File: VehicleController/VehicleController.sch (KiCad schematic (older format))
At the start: 9 parts

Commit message: Updates all around
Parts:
- removed BT?: Battery, symbol Battery
- removed D?: D_Schottky, symbol D_Schottky
- removed F?: Polyfuse, symbol Polyfuse
- removed R? (x3): R, symbol R
- removed U?: TL431, symbol TL431
- removed U?: BTS6133D, symbol BTS6133D
- removed U?: Teensy_3.5, symbol Teensy_3.5
- added C? (x3): C_Small, symbol C_Small
- added J1, J?: RJ45, symbol RJ45
- added P1: CONN_02X02, symbol CONN_02X02
- added P? (x2): CONN_02X12, symbol CONN_02X12
- added P?: CONN_01X02, symbol CONN_01X02
- added U?: Teensy_3.5, symbol Teensy_3.5
- added U?: AP1117, TO_SOT_Packages_SMD:SOT-223, symbol AP1117
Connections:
- net labels added: +12V, +3.3V, +5V, CANH, CANL, CurrentSense
- wire segments 16 -> 38

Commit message: Vehicle Controller updates
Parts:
- removed C? (x2): C_Small, symbol C_Small
- removed J1, J?: RJ45, symbol RJ45
- removed P? (x2): CONN_02X12, symbol CONN_02X12
- removed U?: AP1117, TO_SOT_Packages_SMD:SOT-223, symbol AP1117
- added BT?: Battery_Cell, symbol Battery_Cell
- added C1: C_Small, symbol C_Small
- added P3: RPi_USB_PWR, symbol USB_A
- added P5: SMALL_SIG_MX150, symbol CONN_02X16
- P2: renamed from P?; value CONN_01X02 -> BATT_IN
- gave numbers to parts that had none: 2
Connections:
- net labels added: 3D-FIX, 3D_FIX, CANRX, CANTX, GPS_RX, GPS_TX, SCL0, SDA0
- net labels removed: CANH, CANL
- wire segments 38 -> 45
- no-connect marks 0 -> 5
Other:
- moved on the sheet: C2, P2, U1

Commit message: Added SENtral Fusion Hub to VC Schematic
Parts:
- added U?: UltimateSensorFusion, symbol UltimateSensorFusion
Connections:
- net labels added: CS0, MISO0, MOSI0, SCK0
- wire segments 45 -> 60
- no-connect marks 5 -> 10
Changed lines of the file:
@@
-$EndComp
-$Comp
-L +3.3V #PWR05
-U 1 1 587CCB3B
-P 4200 3900
-F 0 "#PWR05" H 4200 3750 50  0001 C CNN
-F 1 "+3.3V" H 4215 4073 50  0000 C CNN
-F 2 "" H 4200 3900 50  0000 C CNN
-F 3 "" H 4200 3900 50  0000 C CNN
-	1    4200 3900
-	1    0    0    -1
 $EndComp
 $Comp
@@
 Text Label 7100 2800 2    60   ~ 0
 +3.3V
-Text Label 7050 4000 2    60   ~ 0
+Text Label 7400 4000 2    60   ~ 0
 GND
 NoConn ~ 6750 2700
@@
 NoConn ~ 6750 4100
 NoConn ~ 6750 4200
-Text Label 7050 3300 2    60   ~ 0
+Text Label 7100 3300 2    60   ~ 0
 SCL0
-Text Label 7050 3400 2    60   ~ 0
+Text Label 7100 3400 2    60   ~ 0
 SDA0
 Wire Wire Line
@@
 	2400 3300 2400 3400
 Wire Wire Line
-	2050 3300 2400 3300
+	2050 3300 2250 3300
+Wire Wire Line
+	2250 3300 2400 3300
 Wire Wire Line
 	1650 3600 1650 3500
@@
 	2400 3000 2400 2900
 Wire Wire Line
-	2050 3000 2400 3000
-Wire Wire Line
-	4200 4000 4200 3900
-Wire Wire Line
-	4550 4000 4200 4000
+	2050 3000 2250 3000
+Wire Wire Line
+	2250 3000 2400 3000
+Wire Wire Line
+	4550 4000 3550 4000
 Wire Wire Line
 	7350 2600 7350 2650
@@
 Connection ~ 6900 2600
 Wire Wire Line
-	6750 2600 7050 2600
+	6750 2600 6900 2600
+Wire Wire Line
+	6900 2600 7050 2600
 Wire Wire Line
 	6900 2400 6900 2600
@@
 	2300 2150 2400 2150
 Wire Wire Line
-	2400 2050 2400 2250
+	2400 2050 2400 2150
+Wire Wire Line
+	2400 2150 2400 2250
 Wire Wire Line
 	2300 2050 2400 2050
@@
 	1650 2050 1800 2050
 Wire Wire Line
-	1650 1900 1650 2150
+	1650 1900 1650 2050
+Wire Wire Line
+	1650 2050 1650 2150
 Wire Wire Line
 	4200 2600 4550 2600
@@
 	6750 2800 7100 2800
 Wire Wire Line
-	7050 4000 6750 4000
+	7400 4000 6750 4000
 Wire Wire Line
 	4550 3000 4200 3000
@@
 	4550 3100 4200 3100
 Wire Wire Line
-	6750 3300 7050 3300
-Wire Wire Line
-	7050 3400 6750 3400
+	6750 3300 8000 3300
+Wire Wire Line
+	8000 3400 6750 3400
 $Comp
 L Battery_Cell BT?
@@
 Text Label 9400 2200 0    60   ~ 0
 CANRX
+$Comp
+L UltimateSensorFusion U?
+U 1 1 58B0145C
+P 8550 3400
+F 0 "U?" H 8550 3887 60  0000 C CNN
+F 1 "UltimateSensorFusion" H 8550 3781 60  0000 C CNN
+F 2 "" H 8550 3300 60  0001 C CNN
+F 3 "" H 8550 3300 60  0001 C CNN
+	1    8550 3400
+	1    0    0    -1
+$EndComp
+$Comp
+L +3.3V #PWR?
+U 1 1 58B0A4BD
+P 7850 3100
+F 0 "#PWR?" H 7850 2950 50  0001 C CNN
+F 1 "+3.3V" H 7865 3273 50  0000 C CNN
+F 2 "" H 7850 3100 50  0000 C CNN
+F 3 "" H 7850 3100 50  0000 C CNN
+	1    7850 3100
+	1    0    0    -1
+$EndComp
+Wire Wire Line
+	7850 3100 7850 3200
+Wire Wire Line
+	7850 3200 8000 3200
+$Comp
+L GND #PWR?
+U 1 1 58B0C04F
+P 7850 3700
+F 0 "#PWR?" H 7850 3450 50  0001 C CNN
+F 1 "GND" H 7855 3527 50  0000 C CNN
+F 2 "" H 7850 3700 50  0000 C CNN
+F 3 "" H 7850 3700 50  0000 C CNN
+	1    7850 3700
+	1    0    0    -1
+$EndComp
+Wire Wire Line
+	7850 3700 7850 3600
+Wire Wire Line
+	7850 3600 8000 3600
+Wire Wire Line
+	8000 3500 6750 3500
+NoConn ~ 9100 3200
+NoConn ~ 9100 3300
+NoConn ~ 9100 3400
+NoConn ~ 9100 3600
+NoConn ~ 9100 3500
+Text Label 7400 3800 2    60   ~ 0
+CurrentSense
+Wire Wire Line
+	7400 3800 6750 3800
+Wire Wire Line
+	3550 4000 3550 3900
+$Comp
+L +3.3V #PWR05
+U 1 1 587CCB3B
+P 3550 3900
+F 0 "#PWR05" H 3550 3750 50  0001 C CNN
+F 1 "+3.3V" H 3565 4073 50  0000 C CNN
+F 2 "" H 3550 3900 50  0000 C CNN
+F 3 "" H 3550 3900 50  0000 C CNN
+	1    3550 3900
+	1    0    0    -1
+$EndComp
+Wire Wire Line
+	4550 3900 4200 3900
+Text Label 4200 3900 0    60   ~ 0
+MISO0
+Text Label 4200 3800 0    60   ~ 0
+MOSI0
+Text Label 4200 3700 0    60   ~ 0
+CS0
+Wire Wire Line
+	4200 3700 4550 3700
+Wire Wire Line
+	4200 3800 4550 3800
+Wire Wire Line
+	6750 3900 7400 3900
+Text Label 7400 3900 2    60   ~ 0
+SCK0
 $EndSCHEMATC

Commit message: Added GPS, DAC, Isolation sheet, buzzer to VC
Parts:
- removed C1: C_Small, symbol C_Small
- removed P1: CONN_02X02, symbol CONN_02X02
- removed P3: RPi_USB_PWR, symbol USB_A
- added C? (x2): C_Small, symbol C_Small
- added D?: D_Zener, symbol D_Zener
- added F?: 1A, symbol Polyfuse_Small
- added P?: Buzzer, symbol CONN_01X02
- added Q? (x2): Q_NMOS_GDS, symbol Q_NMOS_GDS
- added R? (x4): 2.2k, symbol R_Small
- added R? (x3): R_Small, symbol R_Small
- added U?: BTS6133D, symbol BTS6133D
- BT?: value Battery_Cell -> CR1220
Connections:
- net labels added: +SHTDWN, -SHTDWN, BUZZER, DAC_LATCH, IMU_INT, SCL1, SDA1, SHTDWN_SENSE, SHTDWN_SIG
- net labels removed: 3D-FIX
- wire segments 60 -> 89
- no-connect marks 10 -> 12
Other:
- moved on the sheet: BT?, P5, U?

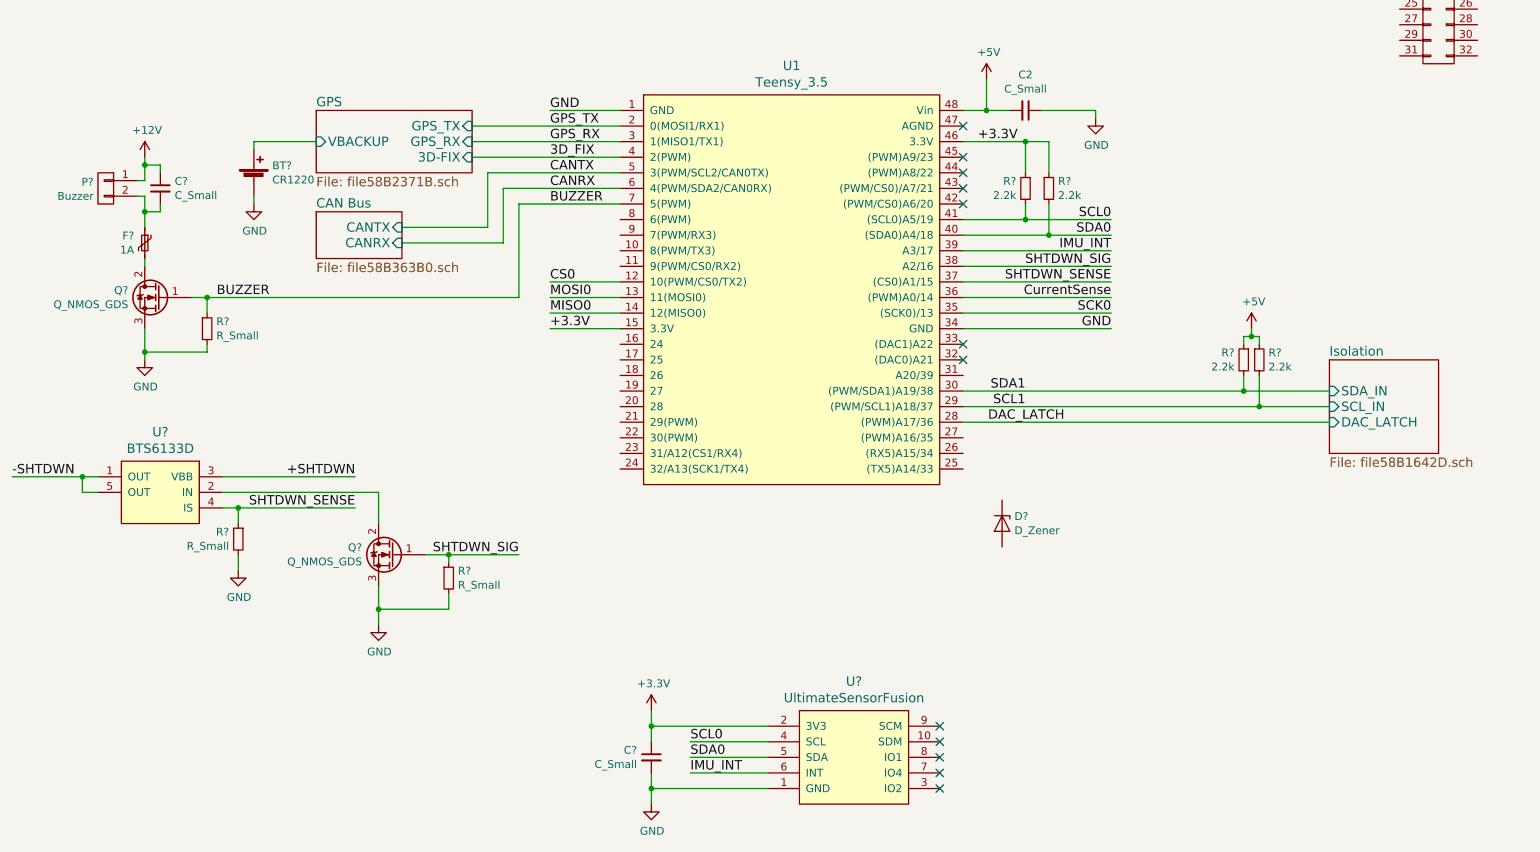
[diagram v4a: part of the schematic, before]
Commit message: Add battery voltage sense, remove i2c pullups for UFS
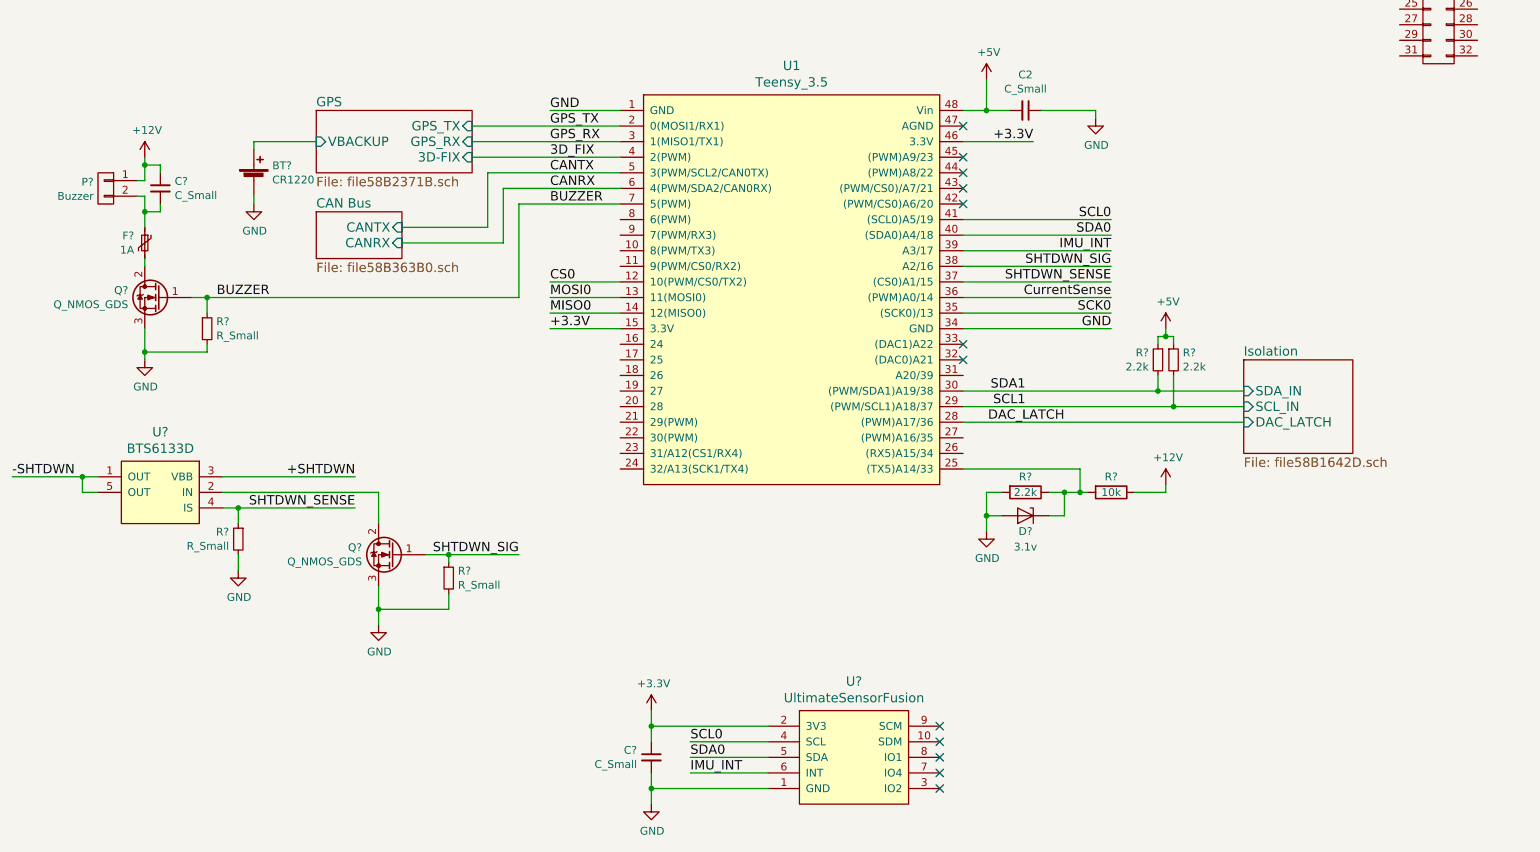
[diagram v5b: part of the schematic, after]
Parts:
- removed D?: D_Zener, symbol D_Zener
- removed R? (x2): 2.2k, symbol R_Small
- added D?: 3.1v, symbol D_Zener
- added R?: 10k, symbol R
- added R?: 2.2k, symbol R
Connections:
- net +12V: now also R?.1
- net GND: now also D?.2 (A), R?.2
- net at U1.25 ((TX5)A14/33): now also D?.1 (K), R?.1, R?.2
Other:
- moved on the sheet: R?

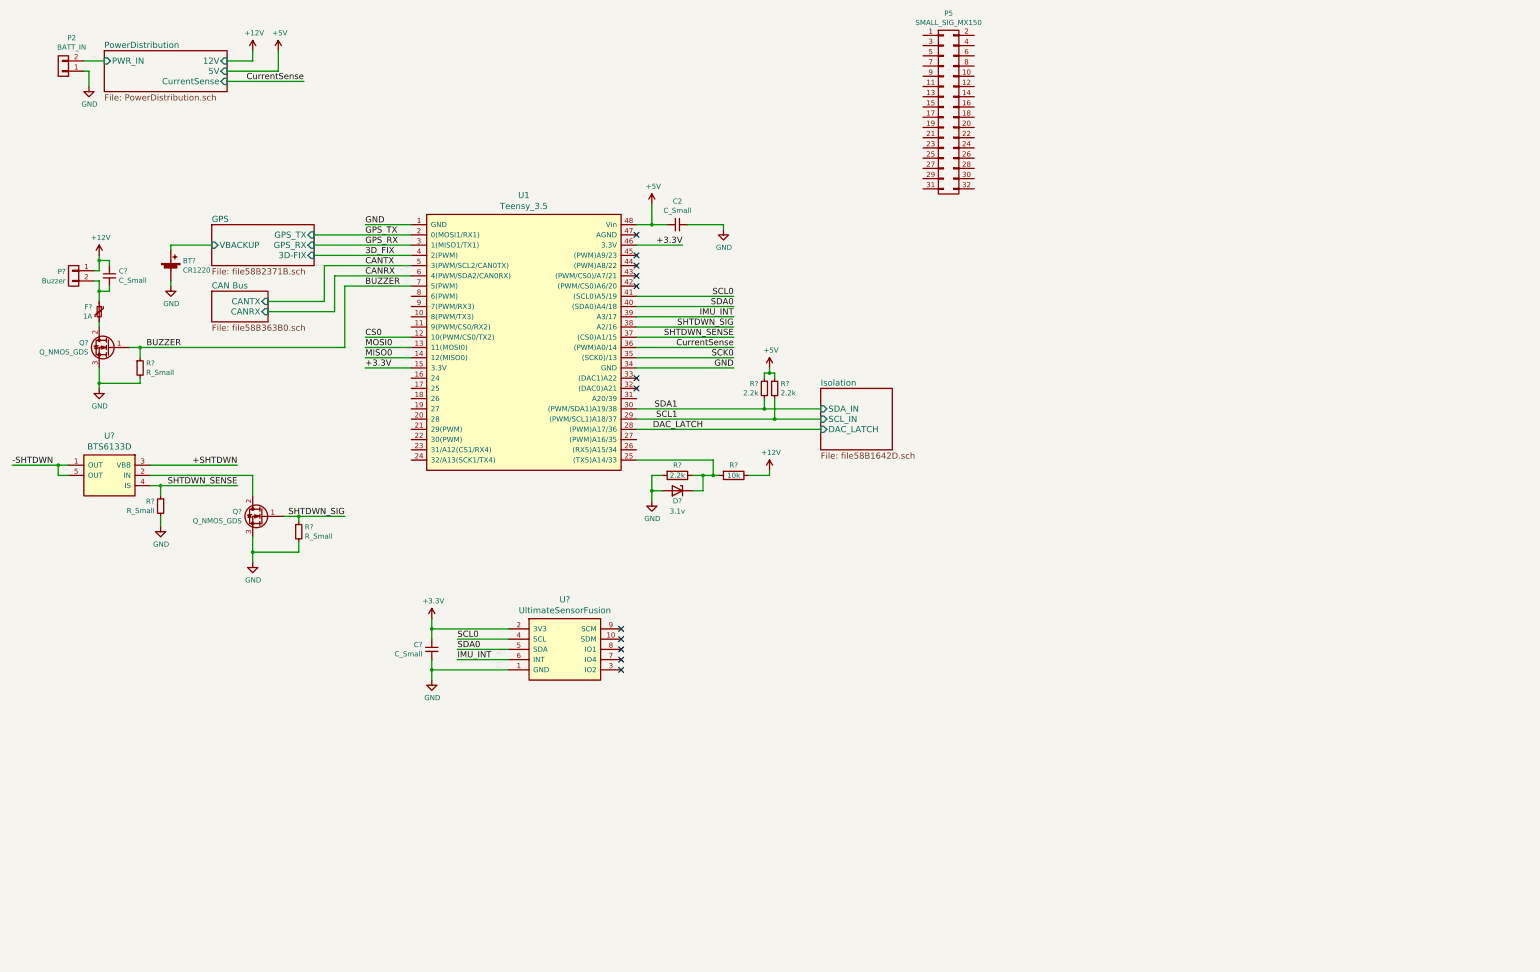
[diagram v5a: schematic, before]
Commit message: 3D model of 16 pin, MX150_8 pin symbol
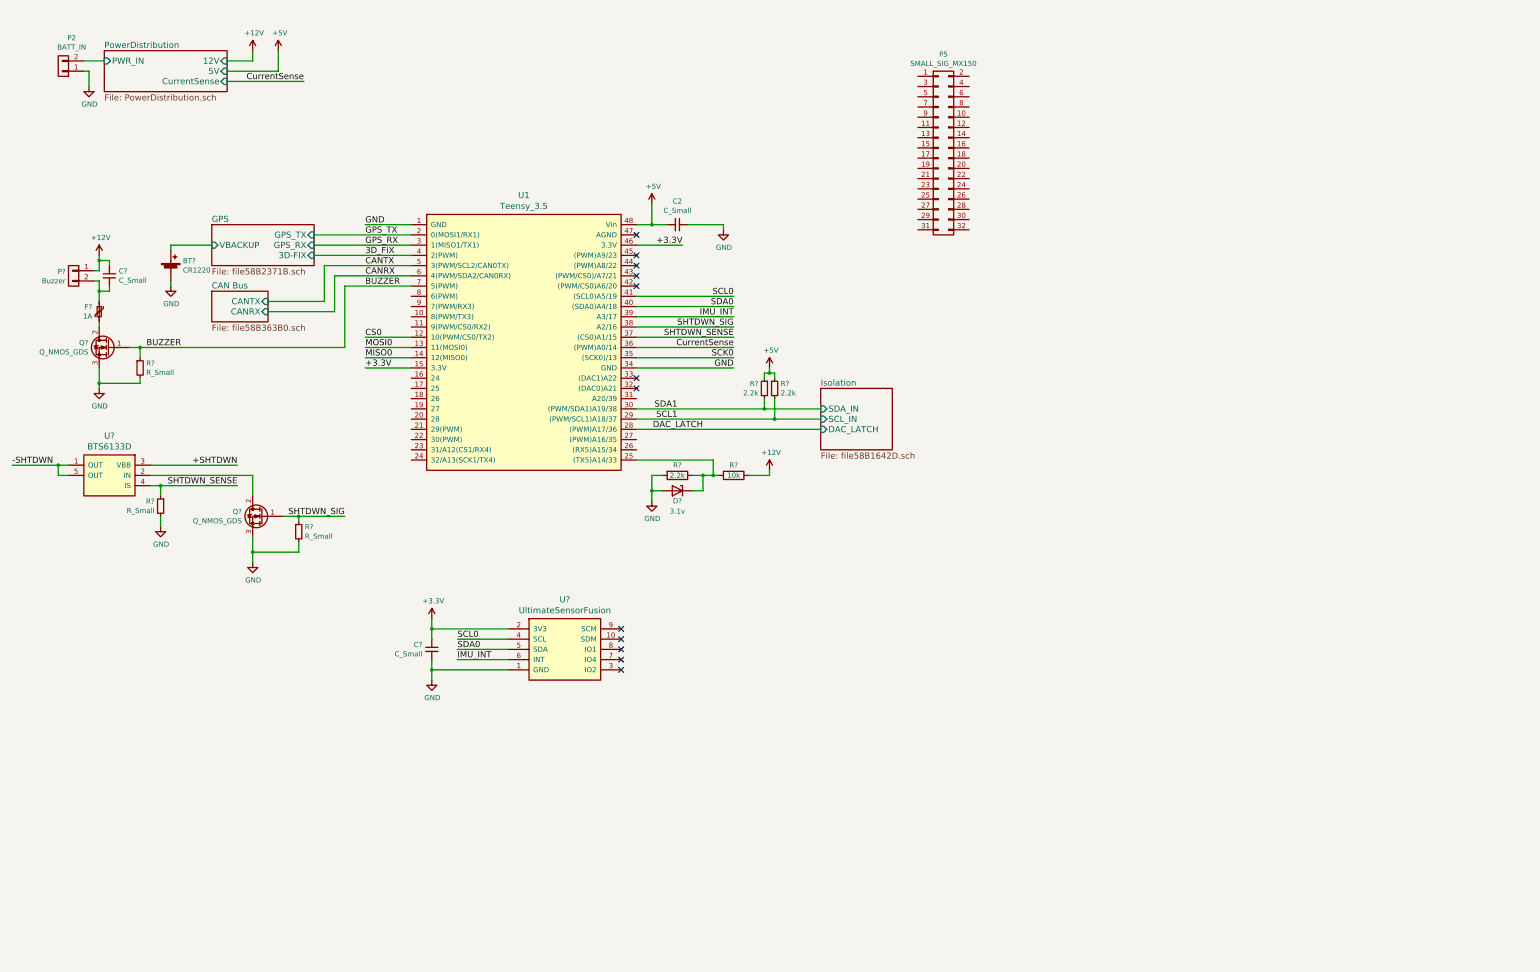
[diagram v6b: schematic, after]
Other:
- moved on the sheet: P5
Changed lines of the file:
@@
 L CONN_02X16 P5
 U 1 1 58AF97B5
-P 9800 1500
-F 0 "P5" H 9800 2465 50  0000 C CNN
-F 1 "SMALL_SIG_MX150" H 9800 2374 50  0000 C CNN
-F 2 "" H 9800 400 50  0000 C CNN
-F 3 "" H 9800 400 50  0000 C CNN
-	1    9800 1500
+P 9750 1900
+F 0 "P5" H 9750 2865 50  0000 C CNN
+F 1 "SMALL_SIG_MX150" H 9750 2774 50  0000 C CNN
+F 2 "" H 9750 800 50  0000 C CNN
+F 3 "" H 9750 800 50  0000 C CNN
+	1    9750 1900
 	1    0    0    -1
 $EndComp
@@
 Connection ~ 6900 2600
 Wire Wire Line
-	6750 2600 6900 2600
-Wire Wire Line
-	6900 2600 7050 2600
+	6750 2600 7050 2600
 Wire Wire Line
 	6900 2400 6900 2600
@@
 	3150 3450 3800 3450
 Wire Wire Line
-	4750 6450 4750 6550
-Wire Wire Line
-	4750 6550 4750 6650
+	4750 6450 4750 6650
 Wire Wire Line
 	4750 6550 5500 6550
 Wire Wire Line
-	4750 6850 4750 6950
-Wire Wire Line
-	4750 6950 4750 7050
+	4750 6850 4750 7050
 Wire Wire Line
 	4750 6950 5500 6950
@@
 	6750 3900 7700 3900
 Wire Wire Line
-	6750 4400 8000 4400
-Wire Wire Line
-	8000 4400 8550 4400
-Wire Wire Line
-	6750 4500 8100 4500
-Wire Wire Line
-	8100 4500 8550 4500
+	6750 4400 8550 4400
+Wire Wire Line
+	6750 4500 8550 4500
 Wire Wire Line
 	6750 4600 8550 4600
 Wire Wire Line
-	8000 4050 8050 4050
-Wire Wire Line
-	8050 4050 8100 4050
+	8000 4050 8100 4050
 Wire Wire Line
 	8100 4050 8100 4100
@@
 Connection ~ 8050 4050
 Wire Wire Line
-	1800 3800 1900 3800
-Wire Wire Line
-	1900 3800 3900 3800
+	1800 3800 3900 3800
 Wire Wire Line
 	1450 3150 1500 3150
 Wire Wire Line
-	1500 3150 1500 3250
-Wire Wire Line
-	1500 3250 1500 3350
-Wire Wire Line
-	1500 4000 1500 4150
-Wire Wire Line
-	1500 4150 1500 4200
+	1500 3150 1500 3350
+Wire Wire Line
+	1500 4000 1500 4200
 Wire Wire Line
 	1500 3600 1500 3600
@@
 	1500 3050 1450 3050
 Wire Wire Line
-	1500 2900 1500 2950
-Wire Wire Line
-	1500 2950 1500 3050
+	1500 2900 1500 3050
 Wire Wire Line
 	3600 2700 4550 2700
@@
 	1500 3550 1500 3600
 Wire Wire Line
-	650  4950 1100 4950
-Wire Wire Line
-	1100 4950 1200 4950
+	650  4950 1200 4950
 Wire Wire Line
 	1200 5050 1100 5050
@@
 	3450 5500 3450 5450
 Wire Wire Line
-	3300 5450 3450 5450
-Wire Wire Line
-	3450 5450 3900 5450
-Wire Wire Line
-	3000 5650 3000 5800
-Wire Wire Line
-	3000 5800 3000 5900
+	3300 5450 3900 5450
+Wire Wire Line
+	3000 5650 3000 5900
 Wire Wire Line
 	3450 5700 3450 5800
@@
 	2100 5250 2100 5150
 Wire Wire Line
-	2000 5150 2100 5150
-Wire Wire Line
-	2100 5150 2850 5150
+	2000 5150 2850 5150
 Wire Wire Line
 	2100 5550 2100 5450
@@
 $EndComp
 Wire Wire Line
-	7300 5050 7400 5050
-Wire Wire Line
-	7400 5050 7500 5050
-Wire Wire Line
-	7500 5050 7550 5050
+	7300 5050 7550 5050
 Wire Wire Line
 	7500 5050 7500 4900
@@
 $EndComp
 Wire Wire Line
-	6900 5050 6900 5200
-Wire Wire Line
-	6900 5200 6900 5300
+	6900 5050 6900 5300
 Wire Wire Line
 	6900 5050 7000 5050

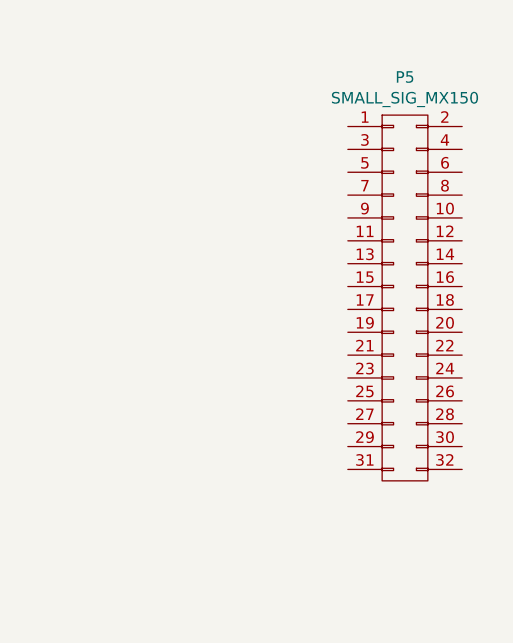
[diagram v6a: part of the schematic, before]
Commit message: Add MX150 8 pin, add Motor Controller connector
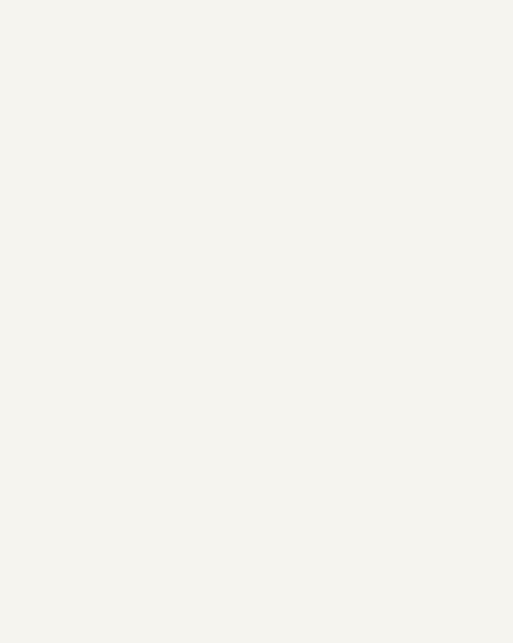
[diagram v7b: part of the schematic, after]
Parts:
- removed P5: SMALL_SIG_MX150, symbol CONN_02X16
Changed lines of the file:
@@
 LIBS:relays
 LIBS:SystemBlocks
+LIBS:dc-dc
+LIBS:Power_Management
 LIBS:VehicleController-cache
 EELAYER 26 0
@@
 	1    0    0    -1
 $EndComp
-$Comp
-L CONN_02X16 P5
-U 1 1 58AF97B5
-P 9750 1900
-F 0 "P5" H 9750 2865 50  0000 C CNN
-F 1 "SMALL_SIG_MX150" H 9750 2774 50  0000 C CNN
-F 2 "" H 9750 800 50  0000 C CNN
-F 3 "" H 9750 800 50  0000 C CNN
-	1    9750 1900
-	1    0    0    -1
-$EndComp
